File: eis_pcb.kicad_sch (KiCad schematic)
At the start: 49 parts, among them J1 Conn_01x01_Socket, J12 104031-0811, J13 10051922-1810ELF, J2 GSB1C41110SSHR, J3 Conn_01x01_Socket, J7 Conn_01x02_Socket, Q3 IRLML6344TRPBF, U1 AD5941BCPZ, U2 ESP32-S3-WROOM-1U-N16R8, U4 MCP73831T-2DCI_OT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

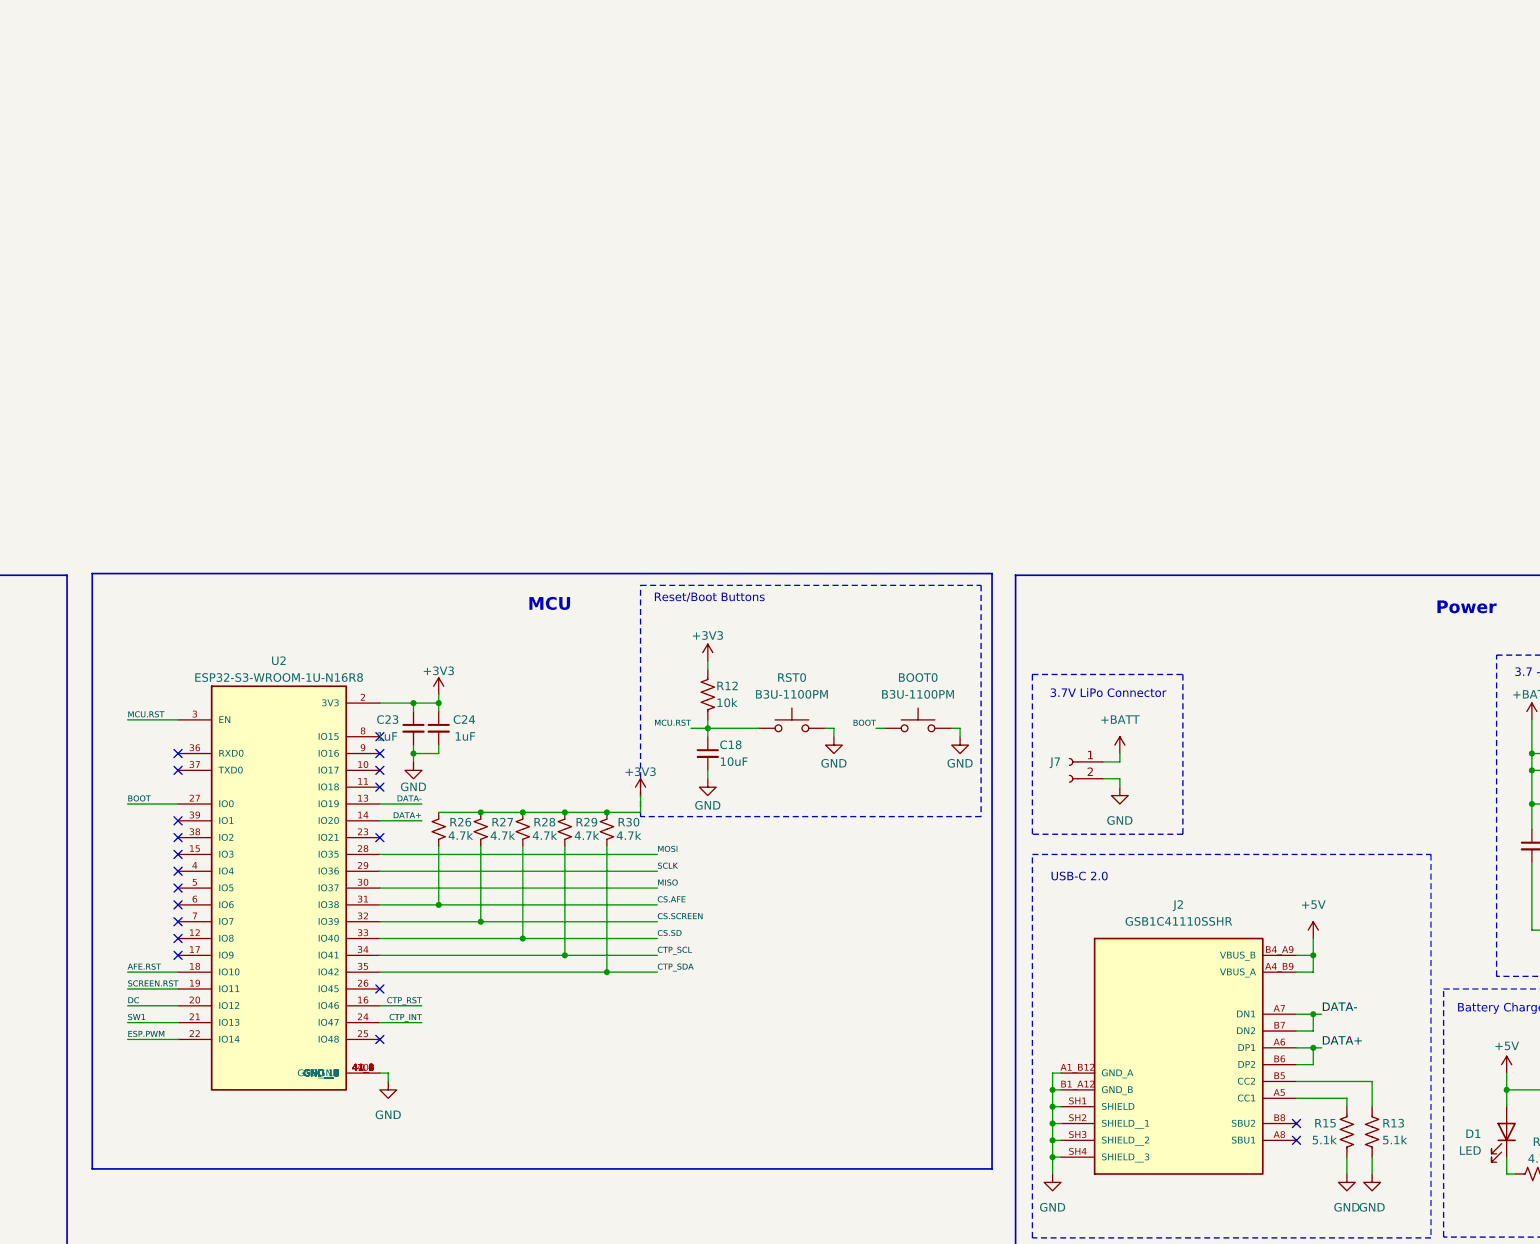
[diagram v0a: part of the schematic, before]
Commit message: Updated to esp+antenna
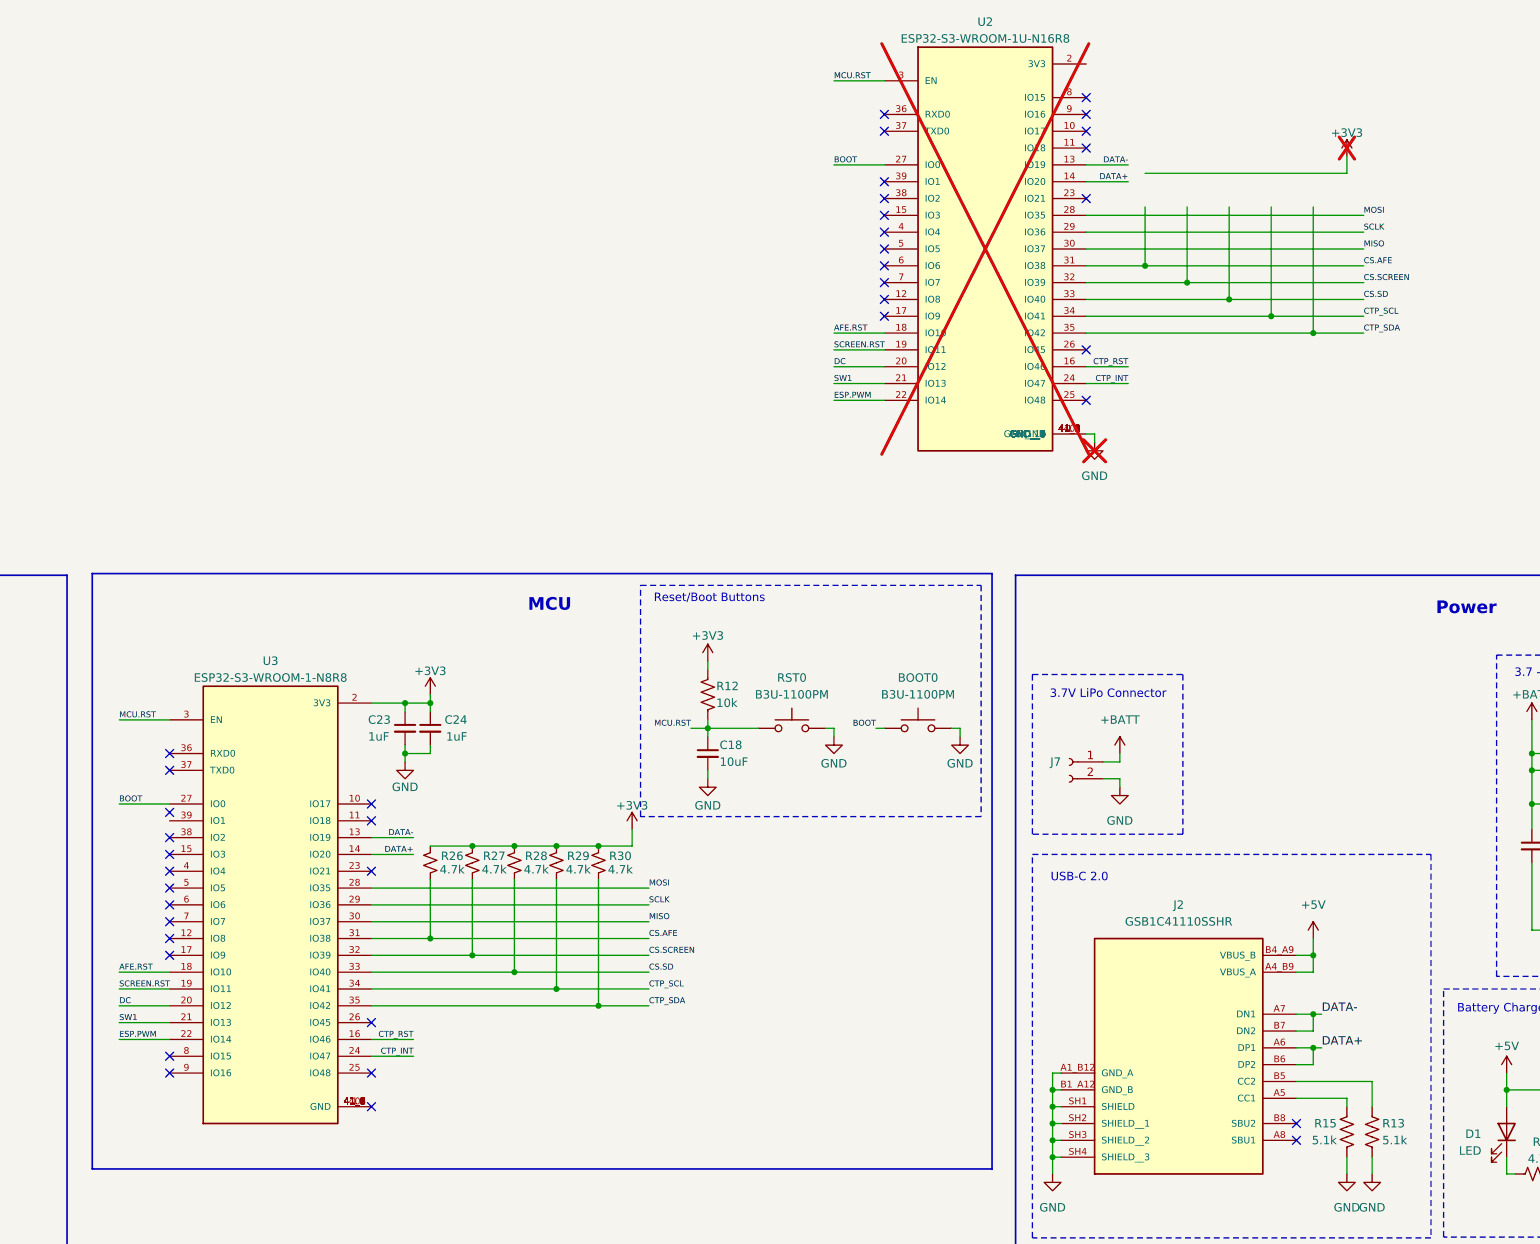
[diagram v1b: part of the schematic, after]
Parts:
- added U3: ESP32-S3-WROOM-1-N8R8, ESP32-S3-WROOM-1-N8R8:XCVR_ESP32S3WROOM1N8R8, symbol ESP32-S3-WROOM-1-N8R8:ESP32-S3-WROOM-1-N8R8
- U2: now not fitted
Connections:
- net +3V3: now also U3.2 (3V3); no longer U2.2 (3V3)
- net AFE.RST: now also U3.18 (IO10)
- net BOOT: now also U3.27 (IO0)
- net CS.AFE: now also U3.31 (IO38)
- net CS.SCREEN: now also U3.32 (IO39)
- net CS.SD: now also U3.33 (IO40)
- net CTP_INT: now also U3.24 (IO47)
- net CTP_RST: now also U3.16 (IO46)
- net CTP_SCL: now also U3.34 (IO41)
- net CTP_SDA: now also U3.35 (IO42)
- net DATA+: now also U3.14 (IO20)
- net DATA-: now also U3.13 (IO19)
- net DC: now also U3.20 (IO12)
- net ESP.PWM: now also U3.22 (IO14)
- net MCU.RST: now also U3.3 (EN)
- net MISO: now also U3.30 (IO37)
- net MOSI: now also U3.28 (IO35)
- net SCLK: now also U3.29 (IO36)
- net SCREEN.RST: now also U3.19 (IO11)
- net SW1: now also U3.21 (IO13)
- new net: U3.1 (GND), U3.40 (GND), U3.41_1 (GND), U3.41_2 (GND), U3.41_3 (GND), U3.41_4 (GND), U3.41_5 (GND), U3.41_6 (GND), U3.41_7 (GND), U3.41_8 (GND), U3.41_9 (GND)
- no-connect marks 41 -> 60
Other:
- moved on the sheet: C23, C24, R26, R27, R28, R29, R30

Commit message: Fixed wiring issues
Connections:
- net GND: now also U3.1 (GND), U3.40 (GND), U3.41_1 (GND), U3.41_2 (GND), U3.41_3 (GND), U3.41_4 (GND), U3.41_5 (GND), U3.41_6 (GND), U3.41_7 (GND), U3.41_8 (GND), U3.41_9 (GND)
- no-connect marks 60 -> 59
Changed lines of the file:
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@@
 	)
 	(no_connect
-		(at 182.88 96.52)
-	)
-	(no_connect
 		(at 260.35 -50.8)
 	)
@@
 	(wire
 		(pts
+			(xy 182.88 96.52) (xy 184.15 96.52)
+		)
+		(stroke
+			(width 0)
+			(type default)
+		)
+	)
+	(wire
+		(pts
 			(xy 201.93 156.21) (xy 201.93 157.48)
 		)
@@
 	(wire
 		(pts
+			(xy 184.15 96.52) (xy 184.15 97.79)
+		)
+		(stroke
+			(width 0)
+			(type default)
+		)
+	)
+	(wire
+		(pts
 			(xy 285.75 101.6) (xy 287.02 101.6)
 		)
@@
 					(unit 1)
 				)
+			)
+		)
+	)
+	(symbol
+		(lib_id "power:GND")
+		(at 184.15 97.79 0)
+		(unit 1)
+		(exclude_from_sim no)
+		(in_bom yes)
+		(on_board yes)
+		(dnp no)
+		(fields_autoplaced yes)
+		(property "Reference" "#PWR01"
+			(at 184.15 104.14 0)
+			(effects
+				(font
+					(size 1.27 1.27)
+				)
+				(hide yes)
+			)
+		)
+		(property "Value" "GND"
+			(at 184.15 102.87 0)
+			(effects
+				(font
+					(size 1.27 1.27)
+				)
+			)
+		)
+		(property "Footprint" ""
+			(at 184.15 97.79 0)
+			(effects
+				(font
+					(size 1.27 1.27)
+				)
+				(hide yes)
+			)
+		)
+		(property "Datasheet" ""
+			(at 184.15 97.79 0)
+			(effects
+				(font
+					(size 1.27 1.27)
+				)
+				(hide yes)
+			)
+		)
+		(property "Description" "Power symbol creates a global label with name \"GND\" , ground"
+			(at 184.15 97.79 0)
+			(effects
+				(font
+					(size 1.27 1.27)
+				)
+				(hide yes)
+			)
+		)
+		(pin "1"
+		)
+		(instances
+			(project ""
+				(path "/b9be45c7-595f-4fac-82ce-4faac3c4812a"
+					(reference "#PWR01")
+					(unit 1)
+				)

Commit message: Improved wiring
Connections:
- net CS.SCREEN: now also U3.16 (IO46); no longer U3.32 (IO39)
- net CTP_INT: now also U3.25 (IO48); no longer U3.24 (IO47)
- net CTP_RST: now also U3.24 (IO47); no longer U3.16 (IO46)
- net DC: now also U3.15 (IO3); no longer U3.20 (IO12)
- net SCREEN.RST: now also U3.23 (IO21); no longer U3.19 (IO11)
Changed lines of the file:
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@@
 	)
 	(junction
+		(at 198.12 86.36)
+		(diameter 0)
+		(color 0 0 0 0)
+	)
+	(junction
 		(at 250.19 140.97)
 		(diameter 0)
@@
 	)
 	(junction
-		(at 198.12 73.66)
-		(diameter 0)
-		(color 0 0 0 0)
-	)
-	(junction
 		(at 81.28 38.1)
 		(diameter 0)
@@
 	)
 	(no_connect
-		(at 182.88 91.44)
-	)
-	(no_connect
 		(at 77.47 68.58)
 	)
@@
 	)
 	(no_connect
+		(at 152.4 81.28)
+	)
+	(no_connect
 		(at 260.35 -50.8)
 	)
@@
 	)
 	(no_connect
-		(at 152.4 58.42)
-	)
-	(no_connect
 		(at 77.47 71.12)
 	)
@@
 	)
 	(no_connect
+		(at 152.4 78.74)
+	)
+	(no_connect
 		(at 391.16 58.42)
 	)
@@
 	)
 	(no_connect
-		(at 152.4 52.07)
-	)
-	(no_connect
 		(at 185.42 163.83)
 	)
 	(no_connect
-		(at 182.88 60.96)
-	)
-	(no_connect
 		(at 182.88 53.34)
 	)
@@
 	)
 	(no_connect
+		(at 152.4 53.34)
+	)
+	(no_connect
+		(at 182.88 73.66)
+	)
+	(no_connect
 		(at 185.42 166.37)
 	)
@@
 	(wire
 		(pts
-			(xy 182.88 73.66) (xy 198.12 73.66)
-		)
-		(stroke
-			(width 0)
-			(type default)
-		)
-	)
-	(wire
-		(pts
 			(xy 110.49 161.29) (xy 107.95 161.29)
 		)
@@
 	(wire
 		(pts
-			(xy 182.88 88.9) (xy 189.23 88.9)
-		)
-		(stroke
-			(width 0)
-			(type default)
-		)
-	)
-	(wire
-		(pts
 			(xy 198.12 156.21) (xy 198.12 157.48)
 		)
@@
 	(wire
 		(pts
+			(xy 182.88 86.36) (xy 198.12 86.36)
+		)
+		(stroke
+			(width 0)
+			(type default)
+		)
+	)
+	(wire
+		(pts
 			(xy 90.17 148.59) (xy 88.9 148.59)
 		)
@@
 	(wire
 		(pts
-			(xy 77.47 43.18) (xy 83.82 43.18)
+			(xy 144.78 58.42) (xy 152.4 58.42)
 		)
 		(stroke
@@
 	(wire
 		(pts
-			(xy 184.15 96.52) (xy 184.15 97.79)
+			(xy 77.47 43.18) (xy 83.82 43.18)
 		)
 		(stroke
@@
 	(wire
 		(pts
-			(xy 285.75 101.6) (xy 287.02 101.6)
+			(xy 184.15 96.52) (xy 184.15 97.79)
 		)
 		(stroke
@@
 	(wire
 		(pts
-			(xy 39.37 157.48) (xy 49.53 157.48)
+			(xy 285.75 101.6) (xy 287.02 101.6)
 		)
 		(stroke
@@
 	(wire
 		(pts
-			(xy 77.47 55.88) (xy 83.82 55.88)
+			(xy 39.37 157.48) (xy 49.53 157.48)
 		)
 		(stroke
@@
 	(wire
 		(pts
-			(xy 144.78 78.74) (xy 152.4 78.74)
+			(xy 77.47 55.88) (xy 83.82 55.88)
 		)
 		(stroke
@@
 	(wire
 		(pts
+			(xy 198.12 86.36) (xy 224.79 86.36)
+		)
+		(stroke
+			(width 0)
+			(type default)
+		)
+	)
+	(wire
+		(pts
 			(xy 252.73 -15.24) (xy 260.35 -15.24)
 		)
@@
 	(wire
 		(pts
+			(xy 198.12 62.23) (xy 198.12 86.36)
+		)
+		(stroke
+			(width 0)
+			(type default)
+		)
+	)
+	(wire
+		(pts
 			(xy 209.55 156.21) (xy 201.93 156.21)
 		)
@@
 	(wire
 		(pts
+			(xy 190.5 60.96) (xy 182.88 60.96)
+		)
+		(stroke
+			(width 0)
+			(type default)
+		)
+	)
+	(wire
+		(pts
 			(xy 322.58 92.71) (xy 334.01 92.71)
 		)
@@
 	(wire
 		(pts
-			(xy 144.78 81.28) (xy 152.4 81.28)
-		)
-		(stroke
-			(width 0)
-			(type default)
-		)
-	)
-	(wire
-		(pts
 			(xy 299.72 -44.45) (xy 330.2 -44.45)
 		)
@@
 	(wire
 		(pts
-			(xy 198.12 73.66) (xy 224.79 73.66)
+			(xy 322.58 90.17) (xy 325.12 90.17)
 		)
 		(stroke
@@
 	(wire
 		(pts
-			(xy 322.58 90.17) (xy 325.12 90.17)
+			(xy 237.49 172.72) (xy 237.49 177.8)
 		)
 		(stroke
@@
 	(wire
 		(pts
-			(xy 237.49 172.72) (xy 237.49 177.8)
+			(xy 182.88 88.9) (xy 189.23 88.9)
 		)
 		(stroke
@@
 	(wire
 		(pts
-			(xy 182.88 86.36) (xy 189.23 86.36)
-		)
-		(stroke
-			(width 0)
-			(type default)
-		)
-	)
-	(wire
-		(pts
 			(xy 77.47 124.46) (xy 78.74 124.46)
 		)
@@
 	(wire
 		(pts
-			(xy 198.12 62.23) (xy 198.12 73.66)
-		)
-		(stroke
-			(width 0)
-			(type default)
-		)
-	)
-	(wire
-		(pts
 			(xy 393.7 50.8) (xy 393.7 45.72)
 		)
@@
 	(wire
 		(pts
+			(xy 182.88 91.44) (xy 189.23 91.44)
+		)
+		(stroke
+			(width 0)
+			(type default)
+		)
+	)
+	(wire
+		(pts
 			(xy 26.67 55.88) (xy 26.67 58.42)
 		)
@@
 		)
 	)
+	(label "CTP_RST"
+		(at 189.23 88.9 180)
+		(effects
+			(font
+				(size 0.889 0.889)
+			)
+			(justify right bottom)
+		)
+	)
 	(label "DC"
 		(at 259.08 151.13 0)
@@
 		)
 	)
-	(label "SCREEN.RST"
-		(at 144.78 78.74 0)
+	(label "CS.SCREEN"
+		(at 259.08 153.67 0)
 		(effects
 			(font
@@
 		)
 	)
-	(label "CS.SCREEN"
-		(at 259.08 153.67 0)
+	(label "DC"
+		(at 144.78 58.42 0)
 		(effects
 			(font
@@
 		)
 	)
-	(label "DC"
-		(at 144.78 81.28 0)
+	(label "CS.SCREEN"
+		(at 224.79 86.36 0)
 		(effects
 			(font
@@
 		)
 	)
+	(label "SCREEN.RST"
+		(at 190.5 60.96 180)
+		(effects
+			(font
+				(size 0.889 0.889)
+			)
+			(justify right bottom)
+		)
+	)
 	(label "BIAS.CAP"
 		(at 58.42 148.59 180)
@@
 		)
 	)
-	(label "CTP_INT"
-		(at 189.23 88.9 180)
-		(effects
-			(font
-				(size 0.889 0.889)
-			)
-			(justify right bottom)
-		)
-	)
 	(label "DATA-"
 		(at 326.39 82.55 0)
@@
 		)
 	)
-	(label "CTP_RST"
-		(at 189.23 86.36 180)
-		(effects
-			(font
-				(size 0.889 0.889)
-			)
-			(justify right bottom)
-		)
-	)
 	(label "BIAS.CAP"
 		(at 83.82 55.88 180)
@@
 		)
 	)
-	(label "CS.SCREEN"
-		(at 224.79 73.66 0)
-		(effects
-			(font
-				(size 0.889 0.889)
-			)
-			(justify left bottom)
-		)
-	)
 	(label "SCLK"
 		(at 224.79 66.04 0)
@@
 		)
 	)
+	(label "CTP_INT"
+		(at 189.23 91.44 180)
+		(effects
+			(font
+				(size 0.889 0.889)
+			)
+			(justify right bottom)
+		)
+	)
